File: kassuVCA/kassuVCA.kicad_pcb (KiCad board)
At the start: 2 copper layers, 74 parts, among them J201 Conn_02x05_Odd_Even, Q401 MBT3904DW1, Q402 MBT3904DW1, Q403 MBT3904DW1, SW401 SW_DPDT_x2, SW402 SW_DPDT_x2, U301 TL074, U401 TL074

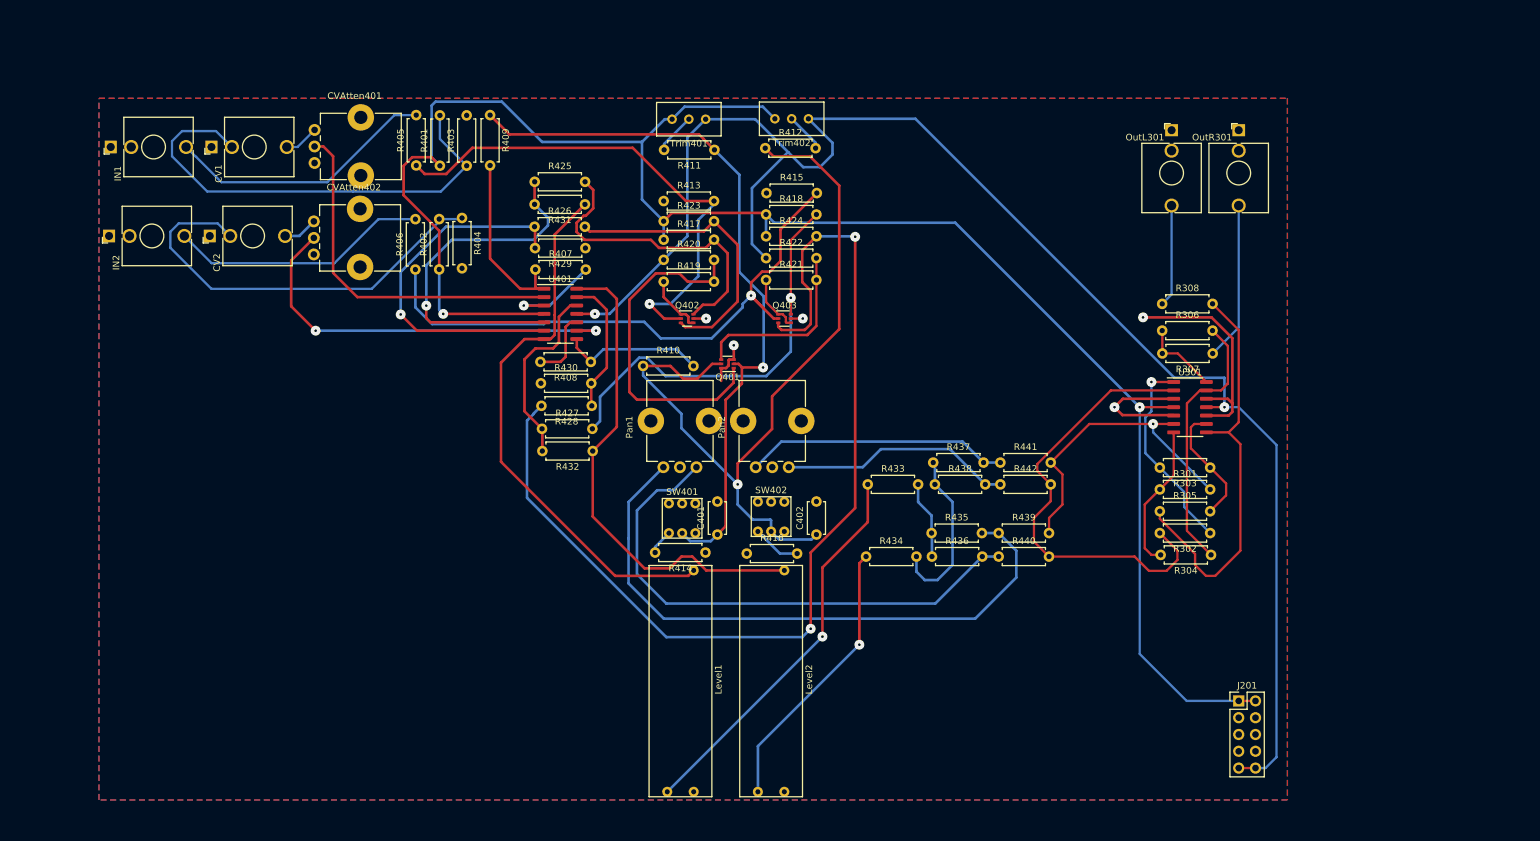
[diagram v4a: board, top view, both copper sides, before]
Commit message: WIP 0805 TL072 dual channel
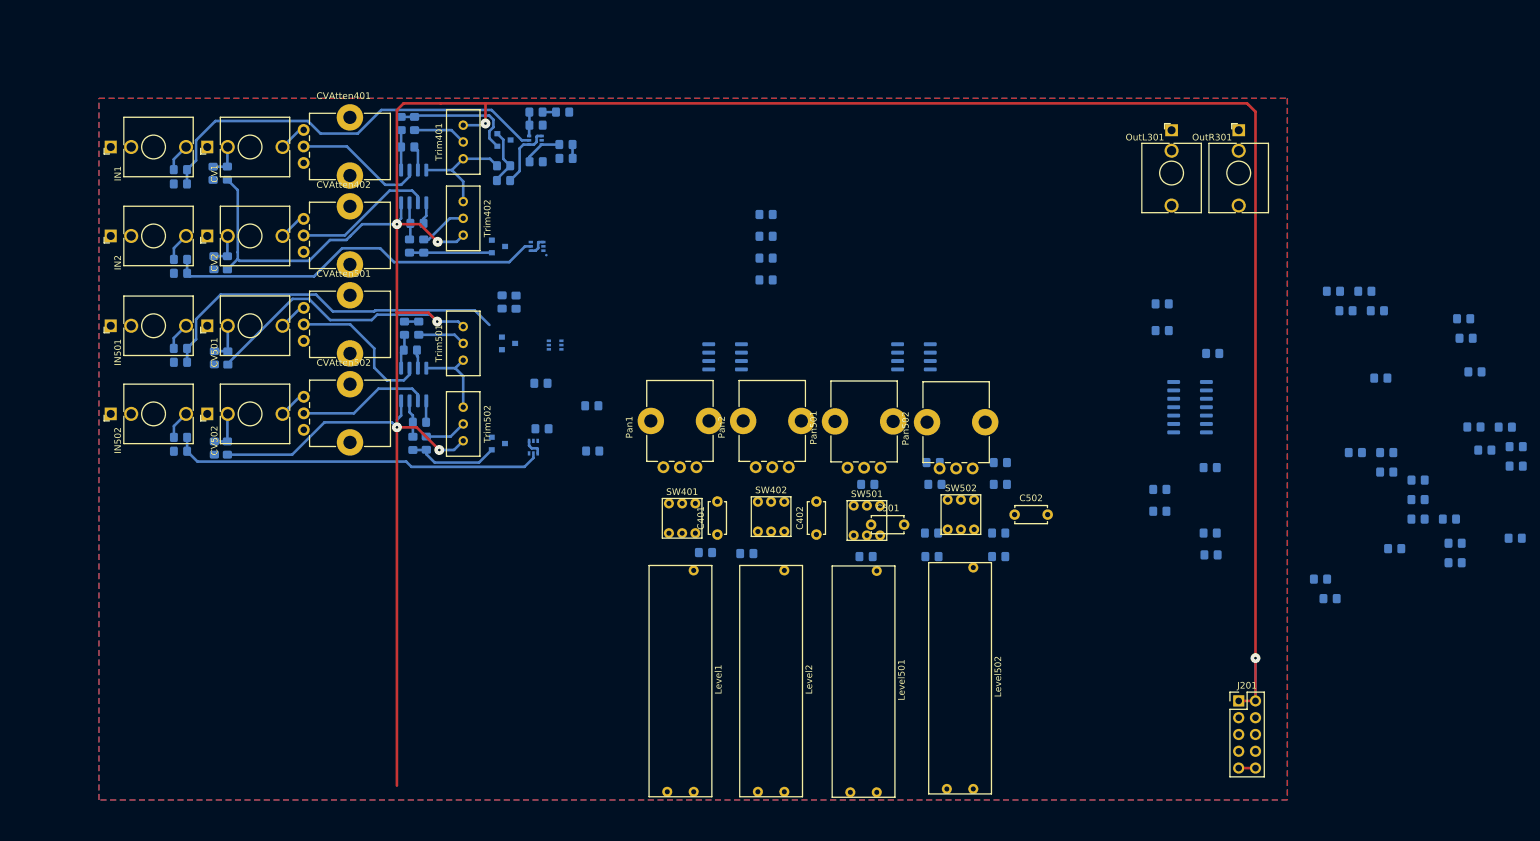
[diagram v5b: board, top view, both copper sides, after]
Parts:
- added C501: C, Capacitor_THT:C_Disc_D4.7mm_W2.5mm_P5.00mm, F.Cu at (142.5, 90.2)
- added C502: C, Capacitor_THT:C_Disc_D4.7mm_W2.5mm_P5.00mm, F.Cu at (164.2, 88.6)
- added CV501: AudioJack2_SwitchT, Connector_Audio:Jack_3.5mm_QingPu_WQP-PJ398SM_Vertical_CircularHoles, F.Cu at (42.0, 60.1)
- added CV502: AudioJack2_SwitchT, Connector_Audio:Jack_3.5mm_QingPu_WQP-PJ398SM_Vertical_CircularHoles, F.Cu at (42.0, 73.4)
- added CVAtten501: 100K, Potentiometer_THT:Potentiometer_Alps_RK09K_Single_Vertical, F.Cu at (56.6, 62.4)
- added CVAtten502: 100K, Potentiometer_THT:Potentiometer_Alps_RK09K_Single_Vertical, F.Cu at (56.6, 75.8)
- added IN501: AudioJack2_SwitchT, Connector_Audio:Jack_3.5mm_QingPu_WQP-PJ398SM_Vertical_CircularHoles, F.Cu at (27.4, 60.1)
- added IN502: AudioJack2_SwitchT, Connector_Audio:Jack_3.5mm_QingPu_WQP-PJ398SM_Vertical_CircularHoles, F.Cu at (27.4, 73.4)
- added Level501: 100K, MixerFootprints:A-1623_SlidePot, F.Cu at (141.4, 113.9)
- added Level502: 100K, MixerFootprints:A-1623_SlidePot, F.Cu at (156.0, 113.4)
- added Pan501: 100K, Potentiometer_THT:Potentiometer_Alps_RK09K_Single_Vertical, F.Cu at (143.9, 81.5)
- added Pan502: 100K, Potentiometer_THT:Potentiometer_Alps_RK09K_Single_Vertical, F.Cu at (157.9, 81.7)
- added Q404: MMBT3904, Package_TO_SOT_SMD:SOT-23, B.Cu at (86.1, 48.1)
- added Q501: MMBT3904, Package_TO_SOT_SMD:SOT-23, B.Cu at (87.6, 62.7)
- added Q502: MMBT3904, Package_TO_SOT_SMD:SOT-23, B.Cu at (86.1, 77.9)
- added Q503: MBT3904DW1, Package_TO_SOT_SMD:SOT-363_SC-70-6, B.Cu at (94.7, 63.0)
- added Q504: MBT3904DW1, Package_TO_SOT_SMD:SOT-363_SC-70-6, B.Cu at (91.4, 78.4)
- added R501: 220K, Resistor_SMD:R_0805_2012Metric_Pad1.20x1.40mm_HandSolder, B.Cu at (45.1, 64.9)
- added R502: 220K, Resistor_SMD:R_0805_2012Metric_Pad1.20x1.40mm_HandSolder, B.Cu at (45.1, 78.6)
- added R503: 100K, Resistor_SMD:R_0805_2012Metric_Pad1.20x1.40mm_HandSolder, B.Cu at (43.1, 64.9)
- added R504: 100K, Resistor_SMD:R_0805_2012Metric_Pad1.20x1.40mm_HandSolder, B.Cu at (43.1, 78.6)
- added R505: 220K, Resistor_SMD:R_0805_2012Metric_Pad1.20x1.40mm_HandSolder, B.Cu at (38.0, 63.5)
- added R506: 220K, Resistor_SMD:R_0805_2012Metric_Pad1.20x1.40mm_HandSolder, B.Cu at (38.0, 77.0)
- added R507: 47K, Resistor_SMD:R_0805_2012Metric_Pad1.20x1.40mm_HandSolder, B.Cu at (72.8, 63.8)
- added R508: 47K, Resistor_SMD:R_0805_2012Metric_Pad1.20x1.40mm_HandSolder, B.Cu at (74.2, 74.7)
- added R509: 22K, Resistor_SMD:R_0805_2012Metric_Pad1.20x1.40mm_HandSolder, B.Cu at (71.9, 60.4)
- added R510: 22K, Resistor_SMD:R_0805_2012Metric_Pad1.20x1.40mm_HandSolder, B.Cu at (73.2, 77.9)
- added R511: 22K, Resistor_SMD:R_0805_2012Metric_Pad1.20x1.40mm_HandSolder, B.Cu at (74.0, 60.4)
- added R512: 22K, Resistor_SMD:R_0805_2012Metric_Pad1.20x1.40mm_HandSolder, B.Cu at (75.2, 77.8)
- added R513: 1K, Resistor_SMD:R_0805_2012Metric_Pad1.20x1.40mm_HandSolder, B.Cu at (38.0, 65.6)
- added R514: 1K, Resistor_SMD:R_0805_2012Metric_Pad1.20x1.40mm_HandSolder, B.Cu at (219.6, 68.0)
- added R515: 1K, Resistor_SMD:R_0805_2012Metric_Pad1.20x1.40mm_HandSolder, B.Cu at (38.0, 79.1)
- added R516: 1K, Resistor_SMD:R_0805_2012Metric_Pad1.20x1.40mm_HandSolder, B.Cu at (210.5, 98.4)
- added R517: 10K, Resistor_SMD:R_0805_2012Metric_Pad1.20x1.40mm_HandSolder, B.Cu at (225.3, 86.4)
- added R518: 10K, Resistor_SMD:R_0805_2012Metric_Pad1.20x1.40mm_HandSolder, B.Cu at (211.9, 101.4)
- added R519: 22K, Resistor_SMD:R_0805_2012Metric_Pad1.20x1.40mm_HandSolder, B.Cu at (88.8, 56.5)
- added R520: 10K, Resistor_SMD:R_0805_2012Metric_Pad1.20x1.40mm_HandSolder, B.Cu at (86.7, 56.5)
- added R521: 22K, Resistor_SMD:R_0805_2012Metric_Pad1.20x1.40mm_HandSolder, B.Cu at (240.1, 81.3)
- added R522: 10K, Resistor_SMD:R_0805_2012Metric_Pad1.20x1.40mm_HandSolder, B.Cu at (214.4, 57.8)
- added R523: 10K, Resistor_SMD:R_0805_2012Metric_Pad1.20x1.40mm_HandSolder, B.Cu at (212.5, 54.9)
- added R524: 10K, Resistor_SMD:R_0805_2012Metric_Pad1.20x1.40mm_HandSolder, B.Cu at (230.9, 93.0)
- added R525: 10K, Resistor_SMD:R_0805_2012Metric_Pad1.20x1.40mm_HandSolder, B.Cu at (220.5, 82.2)
- added R526: 10K, Resistor_SMD:R_0805_2012Metric_Pad1.20x1.40mm_HandSolder, B.Cu at (217.2, 54.9)
- added R527: 10K, Resistor_SMD:R_0805_2012Metric_Pad1.20x1.40mm_HandSolder, B.Cu at (233.7, 75.4)
- added R528: 10K, Resistor_SMD:R_0805_2012Metric_Pad1.20x1.40mm_HandSolder, B.Cu at (225.3, 89.3)
- added R529: 220K, Resistor_SMD:R_0805_2012Metric_Pad1.20x1.40mm_HandSolder, B.Cu at (235.4, 78.9)
- added R530: 220K, Resistor_SMD:R_0805_2012Metric_Pad1.20x1.40mm_HandSolder, B.Cu at (230.9, 95.9)
- added R531: 220K, Resistor_SMD:R_0805_2012Metric_Pad1.20x1.40mm_HandSolder, B.Cu at (221.7, 93.8)
- added R532: 220K, Resistor_SMD:R_0805_2012Metric_Pad1.20x1.40mm_HandSolder, B.Cu at (233.9, 67.0)
- added R533: 220K, Resistor_SMD:R_0805_2012Metric_Pad1.20x1.40mm_HandSolder, B.Cu at (240.0, 92.2)
- added R534: 220K, Resistor_SMD:R_0805_2012Metric_Pad1.20x1.40mm_HandSolder, B.Cu at (240.1, 78.4)
- added R535: 22K, Resistor_SMD:R_0805_2012Metric_Pad1.20x1.40mm_HandSolder, B.Cu at (232.5, 62.0)
- added R536: 22K, Resistor_SMD:R_0805_2012Metric_Pad1.20x1.40mm_HandSolder, B.Cu at (215.8, 79.3)
- added R537: 22K, Resistor_SMD:R_0805_2012Metric_Pad1.20x1.40mm_HandSolder, B.Cu at (230.0, 89.3)
- added R538: 22K, Resistor_SMD:R_0805_2012Metric_Pad1.20x1.40mm_HandSolder, B.Cu at (238.5, 75.4)
- added R539: 22K, Resistor_SMD:R_0805_2012Metric_Pad1.20x1.40mm_HandSolder, B.Cu at (220.5, 79.3)
- added R540: 22K, Resistor_SMD:R_0805_2012Metric_Pad1.20x1.40mm_HandSolder, B.Cu at (225.3, 83.4)
- added R541: 22K, Resistor_SMD:R_0805_2012Metric_Pad1.20x1.40mm_HandSolder, B.Cu at (232.2, 59.0)
- added R542: 22K, Resistor_SMD:R_0805_2012Metric_Pad1.20x1.40mm_HandSolder, B.Cu at (219.1, 57.8)
- added SW501: SW_DPDT_x2, MixerFootprints:A-330-6mm-dpdt, F.Cu at (141.9, 89.5)
- added SW502: SW_DPDT_x2, MixerFootprints:A-330-6mm-dpdt, F.Cu at (156.1, 88.6)
- added Trim501: 100K, Potentiometer_THT:Potentiometer_Bourns_3296W_Vertical, F.Cu at (80.8, 60.2)
- added Trim502: 100K, Potentiometer_THT:Potentiometer_Bourns_3296W_Vertical, F.Cu at (80.8, 77.5)
- added U402: TL072, Package_SO:SOIC-8_3.9x4.9mm_P1.27mm, B.Cu at (120.4, 64.8)
- added U501: TL072, Package_SO:SOIC-8_3.9x4.9mm_P1.27mm, B.Cu at (73.3, 69.0)
- added U502: TL072, Package_SO:SOIC-8_3.9x4.9mm_P1.27mm, B.Cu at (149.0, 64.8)
- Q401: value MBT3904DW1 -> MMBT3904; footprint Package_TO_SOT_SMD:SOT-363_SC-70-6 -> Package_TO_SOT_SMD:SOT-23; moved to B.Cu
- Q402, Q403, U301: moved to B.Cu
- R301, R302, R303, R304, R305, R306, R307, R308, R401, R402, R403, R404, R405, R406, R407, R408, R409, R410, R411, R412, R413, R414, R415, R416, R417, R418, R419, R420, R421, R422, R423, R424, R425, R426, R427, R428, R429, R430, R431, R432, R433, R434, R435, R436, R437, R438, R439, R440, R441, R442: footprint Resistor_THT:R_Axial_DIN0207_L6.3mm_D2.5mm_P7.62mm_Horizontal -> Resistor_SMD:R_0805_2012Metric_Pad1.20x1.40mm_HandSolder; moved to B.Cu
- U401: value TL074 -> TL072; footprint Package_SO:SOIC-14_3.9x8.7mm_P1.27mm -> Package_SO:SOIC-8_3.9x4.9mm_P1.27mm; moved to B.Cu
- moved R415 89.5 mm to (38.0, 52.1)
- moved R413 73.2 mm to (38.0, 38.6)
- moved R412 53.7 mm to (74.8, 48.0), turned to 90 degrees
- moved Trim402 50.3 mm to (80.8, 46.4), turned to 270 degrees
- moved Q401 47.9 mm to (86.9, 32.0), turned to 0 degrees
- moved R411 45.6 mm to (73.4, 29.5), turned to 270 degrees
- moved R410 39.7 mm to (72.6, 48.0), turned to 90 degrees
- moved Q403 39.0 mm to (91.9, 48.1)
- moved R403 38.4 mm to (42.9, 37.0), turned to 270 degrees
- moved R404 38.1 mm to (43.1, 50.5)
- moved R405 35.7 mm to (38.0, 36.4), turned to 180 degrees
- moved R406 35.6 mm to (38.0, 50.0), turned to 180 degrees
- moved Q402 35.4 mm to (91.7, 32.0)
- moved R408 33.6 mm to (73.8, 44.6), turned to 0 degrees
- moved R401 32.2 mm to (45.1, 37.0)
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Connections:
- Q401 pad 1: Net-(Q401-Pad1) -> Net-(C401-Pad1)
- Q401 pad 2: Net-(C401-Pad1) -> Net-(Q401-Pad2)
- R419 pad 2: Net-(Q401-Pad1) -> Net-(Q401-Pad2)
- R420 pad 2: Net-(Q401-Pad1) -> Net-(Q401-Pad2)
- R421 pad 2: Net-(Q401-Pad4) -> Net-(Q404-Pad2)
- R422 pad 2: Net-(Q401-Pad4) -> Net-(Q404-Pad2)
- U401 pad 4: +12V -> -12V
- U401 pad 5: Net-(R425-Pad1) -> Net-(R408-Pad2)
- U401 pad 6: Net-(R426-Pad1) -> Net-(CVAtten402-Pad2)
- U401 pad 7: Net-(Level1-Pad3) -> Net-(R408-Pad1)
- U401 pad 8: Net-(R408-Pad1) -> +12V
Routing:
- net -12V: track 239.8 -> 32.4 mm, vias 2 -> 0
- net +12V: track 281.1 -> 487.4 mm, vias 2 -> 7
- net Net-(Q403-Pad3): track 155.8 -> 0.00 mm, vias 2 -> 0
- net Net-(C402-Pad1): track 121.0 -> 12.5 mm, vias 1 -> 0
- net Net-(Pan1-Pad3): track 93.6 -> 0.00 mm
- net Net-(C401-Pad1): track 109.8 -> 19.1 mm, vias 1 -> 0
- net Net-(Level1-Pad3): track 83.2 -> 0.00 mm
- net Net-(Pan1-Pad1): track 80.9 -> 0.00 mm
- net Net-(Level2-Pad3): track 75.0 -> 0.00 mm
- net Level1L: track 68.3 -> 0.00 mm
- net Net-(CV1-PadTN): track 70.7 -> 5.14 mm
- net Net-(Q403-Pad6): track 64.2 -> 0.00 mm, vias 1 -> 0
- net GND: track 64.0 -> 0.00 mm, vias 5 -> 0
- net Net-(R305-Pad1): track 63.2 -> 0.00 mm
- net Net-(Level1-Pad2): track 59.1 -> 0.00 mm, vias 1 -> 0
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
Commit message: WIP 0805 detangle
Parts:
- moved R521 154.2 mm to (86.1, 73.9), turned to 180 degrees
- moved R524 146.1 mm to (85.1, 82.5)
- moved R529 142.4 mm to (94.9, 55.6), turned to 90 degrees
- moved R530 142.2 mm to (89.2, 84.6)
- moved R517 139.6 mm to (87.2, 65.2), turned to 90 degrees
- moved R525 136.4 mm to (85.2, 65.1), turned to 90 degrees
- moved R528 136.3 mm to (89.2, 82.5), turned to 180 degrees
- moved R532 134.9 mm to (99.1, 71.9)
- moved R527 133.6 mm to (100.1, 75.4), turned to 270 degrees
- moved R522 129.0 mm to (86.1, 71.9), turned to 180 degrees
- moved R531 128.8 mm to (97.3, 60.5)
- moved R526 124.3 mm to (92.9, 55.6), turned to 270 degrees
- moved R523 121.6 mm to (90.9, 55.6), turned to 270 degrees
- moved R518 116.8 mm to (98.0, 75.4), turned to 270 degrees
- moved R541 102.6 mm to (151.1, 121.9), turned to 180 degrees
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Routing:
- net +12V: track 487.4 -> 536.7 mm, vias 7 -> 12
- net GND: track 0.00 -> 33.6 mm, vias 0 -> 6
- net Net-(R528-Pad1): track 0.00 -> 29.3 mm, vias 0 -> 2
- net -12V: track 32.4 -> 57.1 mm, vias 0 -> 2
- net Net-(R426-Pad1): track 2.03 -> 26.0 mm
- net Net-(R526-Pad1): track 0.00 -> 22.2 mm
- net Net-(R525-Pad1): track 0.00 -> 21.7 mm
- net Net-(Q504-Pad6): track 0.00 -> 20.0 mm
- net Net-(Q503-Pad2): track 55.1 -> 71.1 mm
- net Net-(C501-Pad1): track 2.16 -> 16.1 mm
- net Net-(Q503-Pad1): track 0.00 -> 13.2 mm
- net Net-(Level1-Pad3): track 0.00 -> 12.3 mm
- net Net-(Q403-Pad1): track 2.91 -> 14.0 mm, vias 0 -> 2
- net Net-(Q403-Pad6): track 0.00 -> 10.0 mm
- net Net-(R425-Pad1): track 2.14 -> 12.2 mm
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
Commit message: 4/6 channels, 4 routed
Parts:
- moved R441 64.1 mm to (122.3, 77.2), turned to 270 degrees
- moved R535 51.4 mm to (136.4, 72.9)
- moved R442 50.4 mm to (132.3, 77.2), turned to 270 degrees
- moved R438 50.1 mm to (132.3, 73.2), turned to 270 degrees
- moved R436 49.8 mm to (118.3, 73.2), turned to 270 degrees
- moved R537 49.4 mm to (150.1, 72.8), turned to 270 degrees
- moved R538 47.4 mm to (160.4, 72.8), turned to 270 degrees
- moved R539 47.2 mm to (136.4, 76.8), turned to 270 degrees
- moved R435 47.1 mm to (108.6, 73.2), turned to 270 degrees
- moved R437 47.1 mm to (122.3, 73.2), turned to 270 degrees
- moved R440 46.5 mm to (118.3, 77.2), turned to 270 degrees
- moved R533 45.3 mm to (136.4, 80.8), turned to 90 degrees
- moved R541 45.2 mm to (150.1, 76.7), turned to 270 degrees
- moved R434 44.8 mm to (122.3, 81.1), turned to 90 degrees
- moved R433 43.8 mm to (108.6, 81.6), turned to 90 degrees
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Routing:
- net -12V: track 57.1 -> 382.8 mm, vias 2 -> 7
- net Level1R: track 0.00 -> 162.4 mm, vias 0 -> 5
- net Level1L: track 0.00 -> 149.0 mm, vias 0 -> 6
- net Net-(C501-Pad1): track 16.1 -> 117.3 mm, vias 0 -> 1
- net Net-(C401-Pad1): track 19.8 -> 117.2 mm, vias 0 -> 1
- net Net-(C502-Pad1): track 17.5 -> 113.8 mm, vias 0 -> 1
- net +12V: track 536.7 -> 625.5 mm, vias 12 -> 10
- net Net-(C402-Pad1): track 12.5 -> 100.5 mm, vias 0 -> 1
- net Net-(Level502-Pad3): track 3.64 -> 90.8 mm, vias 0 -> 2
- net Net-(Level2-Pad3): track 3.77 -> 82.7 mm, vias 0 -> 2
- net Net-(Level501-Pad3): track 3.17 -> 80.9 mm
- net GND: track 33.6 -> 106.1 mm, vias 6 -> 18
- net Net-(Level1-Pad3): track 12.3 -> 74.1 mm
- net Net-(Level502-Pad2): track 0.00 -> 50.1 mm, vias 0 -> 2
- net Net-(Level501-Pad2): track 0.00 -> 49.6 mm, vias 0 -> 2
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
